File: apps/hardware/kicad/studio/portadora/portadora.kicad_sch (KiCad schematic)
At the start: 56 parts, among them J1 Teensy 4.1 izq, J10 USB-C 5V 3A, J11 OUT L 6.35, J12 OUT R 6.35, J13 PHONES 3.5 sleeve HP_VGND, J14 CV OUT 3.5, J2 Teensy 4.1 der, J3 USB host Teensy, J4 USB-A host, J5 Panel IDC 2x15, J6 Raspberry Pi pines 1-10, J7 IN L 6.35, J8 IN R 6.35, J9 Audio Shield LINE y HP, SW1 PAD 0 -10 -20 dB, U1 74AHCT1G125, U2 MCP6004

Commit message: feat(hardware): portadora con shield lado a lado y etapa de entrada validada por simulación
- Alimentación por JST-XH (J10) desde una placa USB-C de panel; USB-A host y USB de datos van
  en la tapa trasera con extensiones (se quitan J4, R1, R2).
- Audio Shield Rev D lado a lado, no apilado: zócalos J15/J16 que solo cablean 7, 8, 18–21, 23,
  3V3 y GND. Los pines 10–13 y 15 (encoders) quedan aislados del slot SD y del MEM.
- Etapa de entrada (theory/03-studio-input-stage.md): la escalera del pad se recalcula con la carga
  de R10+R12 (R5/R8 12.4k, R6/R9 5.23k) y el RC del CV OUT baja a 4.7k (1 % en 5 ms).
- Plan B: JP2–JP5 para saltar el MCP6004 si hiciera falta, y TP1–TP5 para diagnóstico.
- sim/input_stage_sim.py: ngspice de KiCad. Lee valores y topología del esquemático y verifica
  C1–C6; los seis pasan (sim/results.md).

Co-Authored-By: Claude Opus 5.5 <noreply@anthropic.com>
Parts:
- removed J10: USB-C 5V 3A, Connector_USB:USB_C_Receptacle_GCT_USB4125-xx-x_6P_TopMnt_Horizontal, symbol Connector:USB_C_Receptacle_PowerOnly_6P
- removed J4: USB-A host, Connector_USB:USB_A_Molex_67643_Horizontal, symbol Connector:USB_A
- removed R1, R2: 5.1k, Resistor_SMD:R_0603_1608Metric, symbol Device:R
- added J10: 5V desde USB-C de panel, Connector_JST:JST_XH_B2B-XH-A_1x02_P2.50mm_Vertical, symbol Connector_Generic:Conn_01x02
- added J15: Shield fila 13-5V, Connector_PinSocket_2.54mm:PinSocket_1x14_P2.54mm_Vertical, symbol Connector_Generic:Conn_01x14
- added J16: Shield fila 12-GND, Connector_PinSocket_2.54mm:PinSocket_1x14_P2.54mm_Vertical, symbol Connector_Generic:Conn_01x14
- added JP2: BYP L (sin U2), Jumper:SolderJumper-2_P1.3mm_Open_RoundedPad1.0x1.5mm, symbol Jumper:SolderJumper_2_Open
- added JP3: BYP R (sin U2), Jumper:SolderJumper-2_P1.3mm_Open_RoundedPad1.0x1.5mm, symbol Jumper:SolderJumper_2_Open
- added JP4: BYP VREF (sin U2), Jumper:SolderJumper-2_P1.3mm_Open_RoundedPad1.0x1.5mm, symbol Jumper:SolderJumper_2_Open
- added JP5: BYP CV (sin U2), Jumper:SolderJumper-2_P1.3mm_Open_RoundedPad1.0x1.5mm, symbol Jumper:SolderJumper_2_Open
- added TP1: VREF, TestPoint:TestPoint_Pad_D1.5mm, symbol Connector:TestPoint
- added TP2: BUF_L, TestPoint:TestPoint_Pad_D1.5mm, symbol Connector:TestPoint
- added TP3: BUF_R, TestPoint:TestPoint_Pad_D1.5mm, symbol Connector:TestPoint
- added TP4: CV_BUF, TestPoint:TestPoint_Pad_D1.5mm, symbol Connector:TestPoint
- added TP5: GND, TestPoint:TestPoint_Pad_D1.5mm, symbol Connector:TestPoint
- R18, R19: value 10k -> 4.7k
- R5, R8: value 10.2k -> 12.4k
- R6, R9: value 4.75k -> 5.23k
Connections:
- net +3V3: now also J15.12 (Pin_12)
- net BUF_L: now also JP2.2 (B), TP2.1
- net BUF_R: now also JP3.2 (B), TP3.1
- net CV_BUF: now also JP5.2 (B), TP4.1
- net CV_FILT: now also JP5.1 (A)
- net GND: now also J10.2 (Pin_2), J15.13 (Pin_13), J16.14 (Pin_14), TP5.1
- net PROT_L: now also JP2.1 (A)
- net PROT_R: now also JP3.1 (A)
- net VBUS_IN: now also J10.1 (Pin_1)
- net VREF: now also JP4.2 (B), TP1.1
- net VREF_DIV: now also JP4.1 (A)
- net I2S_MCLK: now reaches J2.4 (Pin_4)
- net I2S_MCLK: now also J15.11 (Pin_11)
- net I2S_BCLK: now reaches J2.6 (Pin_6)
- net I2S_BCLK: now also J15.9 (Pin_9)
- net I2S_LRCLK: now reaches J2.7 (Pin_7)
- net I2S_LRCLK: now also J15.8 (Pin_8)
- net I2C_SCL: now reaches J2.8 (Pin_8)
- net I2C_SCL: now also J15.7 (Pin_7)
- net I2C_SDA: now reaches J2.9 (Pin_9)
- net I2C_SDA: now also J15.6 (Pin_6)
- net I2S_RX: now reaches J1.10 (Pin_10)
- net I2S_RX: now also J16.5 (Pin_5)
- net I2S_TX: now reaches J1.9 (Pin_9)
- net I2S_TX: now also J16.6 (Pin_6)
- no-connect marks 20 -> 31
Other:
- note added: "NOTAS 1. Teensy 4.1: CORTAR el puente VUSB–VIN. Todo se alimenta de J10 (JST-XH desde una placa USB-C de panel, solo 5 V, con sus 5.1 kΩ en CC); el USB de la Teensy queda solo para datos (y MIDI por USB). 2. USB en la tapa trasera: USB-C de datos = extensión de panel a la micro-USB de la Teensy; USB-A host = extensión de panel a J3. J1/J2 = las dos filas de la Teensy (vista superior, USB arriba).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"
- note added: "PLAN B DE LA ETAPA DE ENTRADA (theory/03-studio-input-stage.md §6) JP2–JP5 abiertos de fábrica. Cerrarlos SOLO con U2 retirado o pedido DNP: un jumper cerrado con U2 montado une la salida del seguidor con su entrada. Diagnóstico sin señal: TP1 VREF, TP2 BUF_L y TP3 BUF_R = 1.65 V; TP4 sigue al duty del pin 29."
- note removed: "NOTAS 1. Teensy 4.1: CORTAR el puente VUSB–VIN de la Teensy. Todo se alimenta del USB-C de J10; el USB de la Teensy queda solo para datos (y MIDI por USB). 2. J1/J2 = las dos filas de la Teensy (vista superior, USB arriba). Izq: GND,0–12,3V3,24–32. Der: VIN,GND,3V3,23–13,GND,41–33. Los pines del Audio Shield (6,7,8,18,19,20,21,23) van por el apilado Teensy+Shield y quedan sin conexión en esta pla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"

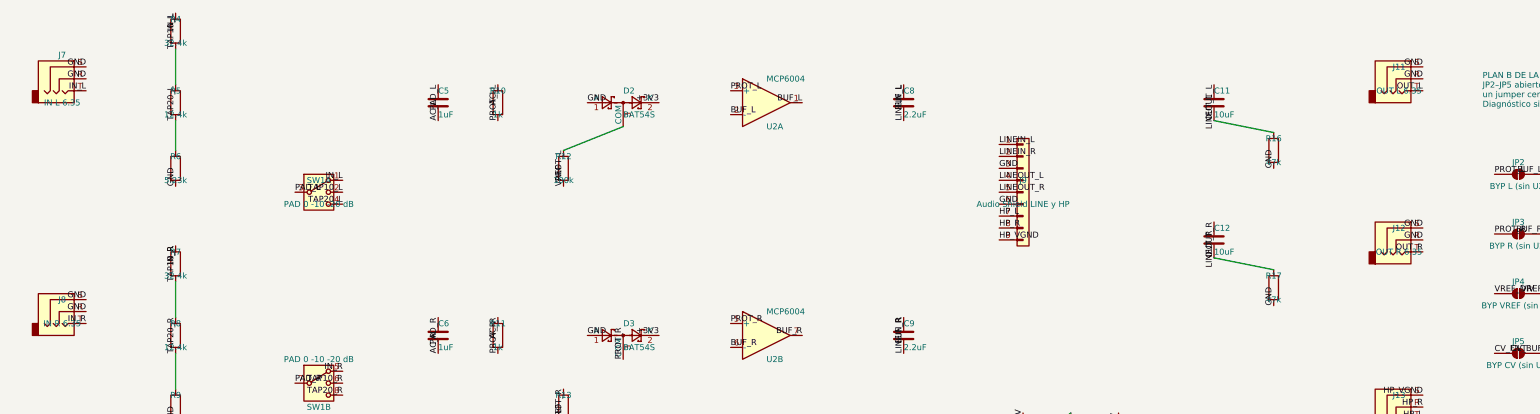
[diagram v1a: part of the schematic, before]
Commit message: feat(hardware): enclosure +15 mm, PCB-A de una cara y ubicación de la portadora
Enclosure (design/README.md, theory/02 §3 y §4.3–4.5), medido el módulo Freenove con la Pi:
- Cuña de 43/78 mm (+15 mm parejo, 12°): la portadora entra bajo la Pi con margen y hay más aire.
- Pantalla corrida 2.5 mm hacia atrás (centro y 114.9): el vidrio (120.8 × 76 × 7.6 mm) ya no se monta
  sobre PCB-K; ranuras de aire en y 155–165.
- Pi atornillada detrás de la Freenove, puertos hacia la derecha (adentro): se elimina la tapa de servicio.
- Jacks en una hilera baja soldados a la portadora (1/4" NRJ3HF-1); USB y palanca PAD de panel arriba.
  La placa trasera vertical se descartó antes de commit.

PCB-A: todos los SMD en la cara superior (ensamble Economic de una cara); vía propia para los GND del
JST; re-ruteada. DRC 0/0.

Portadora: tools/place_portadora.py (97 × 100 mm, jacks contra la pared, shield y entrada analógica al
medio, Teensy y alimentación adelante, J5/J6 al frente). DRC con paridad: 0 violaciones; falta rutear.
Herramientas: costura de GND que respeta agujeros e islas, route_board sin duplicar lo bloqueado,
sync_fp_fields con redes "unconnected" y atributos de BOM, trim_silk_outside.py.

Co-Authored-By: Claude Opus 5.5 <noreply@anthropic.com>
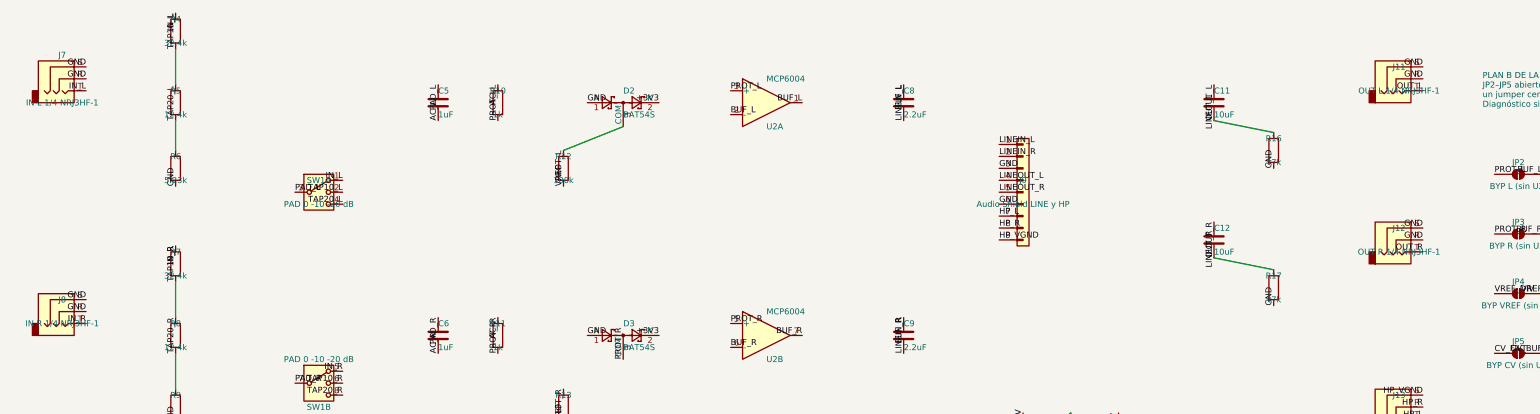
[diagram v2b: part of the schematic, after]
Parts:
- J11: value OUT L 6.35 -> OUT L 1/4 NRJ3HF-1; footprint Connector_Audio:Jack_6.35mm_Neutrik_NMJ6HFD2_Horizontal -> Connector_Audio:Jack_6.35mm_Neutrik_NRJ3HF-1_Horizontal
- J12: value OUT R 6.35 -> OUT R 1/4 NRJ3HF-1; footprint Connector_Audio:Jack_6.35mm_Neutrik_NMJ6HFD2_Horizontal -> Connector_Audio:Jack_6.35mm_Neutrik_NRJ3HF-1_Horizontal
- J7: value IN L 6.35 -> IN L 1/4 NRJ3HF-1; footprint Connector_Audio:Jack_6.35mm_Neutrik_NMJ6HFD2_Horizontal -> Connector_Audio:Jack_6.35mm_Neutrik_NRJ3HF-1_Horizontal
- J8: value IN R 6.35 -> IN R 1/4 NRJ3HF-1; footprint Connector_Audio:Jack_6.35mm_Neutrik_NMJ6HFD2_Horizontal -> Connector_Audio:Jack_6.35mm_Neutrik_NRJ3HF-1_Horizontal
- JP1, JP2, JP3, JP4, JP5, TP1, TP2, TP3, TP4, TP5: now left out of the parts list
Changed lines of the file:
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@@
 		(body_style 1)
 		(exclude_from_sim no)
-		(in_bom yes)
+		(in_bom no)
 		(on_board yes)
-		(in_pos_files yes)
+		(in_pos_files no)
 		(dnp no)
 		(property "Reference" "JP1"
@@
 			)
 		)
-		(property "Value" "IN L 6.35"
+		(property "Value" "IN L 1/4 NRJ3HF-1"
 			(at 25.4 185.42 0)
 			(show_name no)
@@
 			)
 		)
-		(property "Footprint" "Connector_Audio:Jack_6.35mm_Neutrik_NMJ6HFD2_Horizontal"
+		(property "Footprint" "Connector_Audio:Jack_6.35mm_Neutrik_NRJ3HF-1_Horizontal"
 			(at 25.4 180.34 0)
 			(hide yes)
@@
 			)
 		)
-		(property "Value" "IN R 6.35"
+		(property "Value" "IN R 1/4 NRJ3HF-1"
 			(at 25.4 232.41 0)
 			(show_name no)
@@
 			)
 		)
-		(property "Footprint" "Connector_Audio:Jack_6.35mm_Neutrik_NMJ6HFD2_Horizontal"
+		(property "Footprint" "Connector_Audio:Jack_6.35mm_Neutrik_NRJ3HF-1_Horizontal"
 			(at 25.4 229.87 0)
 			(hide yes)
@@
 			)
 		)
-		(property "Value" "OUT L 6.35"
+		(property "Value" "OUT L 1/4 NRJ3HF-1"
 			(at 309.88 182.88 0)
 			(show_name no)
@@
 			)
 		)
-		(property "Footprint" "Connector_Audio:Jack_6.35mm_Neutrik_NMJ6HFD2_Horizontal"
+		(property "Footprint" "Connector_Audio:Jack_6.35mm_Neutrik_NRJ3HF-1_Horizontal"
 			(at 309.88 180.34 0)
 			(hide yes)
@@
 			)
 		)
-		(property "Value" "OUT R 6.35"
+		(property "Value" "OUT R 1/4 NRJ3HF-1"
 			(at 309.88 217.17 0)
 			(show_name no)
@@
 			)
 		)
-		(property "Footprint" "Connector_Audio:Jack_6.35mm_Neutrik_NMJ6HFD2_Horizontal"
+		(property "Footprint" "Connector_Audio:Jack_6.35mm_Neutrik_NRJ3HF-1_Horizontal"
 			(at 309.88 214.63 0)
 			(hide yes)
@@
 		(body_style 1)
 		(exclude_from_sim no)
-		(in_bom yes)
+		(in_bom no)
 		(on_board yes)
-		(in_pos_files yes)
+		(in_pos_files no)
 		(dnp no)
 		(property "Reference" "JP2"
@@
 		(body_style 1)
 		(exclude_from_sim no)
-		(in_bom yes)
+		(in_bom no)
 		(on_board yes)
-		(in_pos_files yes)
+		(in_pos_files no)
 		(dnp no)
 		(property "Reference" "JP3"
@@
 		(body_style 1)
 		(exclude_from_sim no)
-		(in_bom yes)
+		(in_bom no)
 		(on_board yes)
-		(in_pos_files yes)
+		(in_pos_files no)
 		(dnp no)
 		(property "Reference" "JP4"
@@
 		(body_style 1)
 		(exclude_from_sim no)
-		(in_bom yes)
+		(in_bom no)
 		(on_board yes)
-		(in_pos_files yes)
+		(in_pos_files no)
 		(dnp no)
 		(property "Reference" "JP5"
@@
 		(body_style 1)
 		(exclude_from_sim no)
-		(in_bom yes)
+		(in_bom no)
 		(on_board yes)
-		(in_pos_files yes)
+		(in_pos_files no)
 		(dnp no)
 		(property "Reference" "TP1"
@@
 		(body_style 1)
 		(exclude_from_sim no)
-		(in_bom yes)
+		(in_bom no)
 		(on_board yes)
-		(in_pos_files yes)
+		(in_pos_files no)
 		(dnp no)
 		(property "Reference" "TP2"
@@
 		(body_style 1)
 		(exclude_from_sim no)
-		(in_bom yes)
+		(in_bom no)
 		(on_board yes)
-		(in_pos_files yes)
+		(in_pos_files no)
 		(dnp no)
 		(property "Reference" "TP3"
@@
 		(body_style 1)
 		(exclude_from_sim no)
-		(in_bom yes)
+		(in_bom no)
 		(on_board yes)
-		(in_pos_files yes)
+		(in_pos_files no)
 		(dnp no)
 		(property "Reference" "TP4"
@@
 		(body_style 1)
 		(exclude_from_sim no)
-		(in_bom yes)
+		(in_bom no)
 		(on_board yes)
-		(in_pos_files yes)
+		(in_pos_files no)
 		(dnp no)
 		(property "Reference" "TP5"

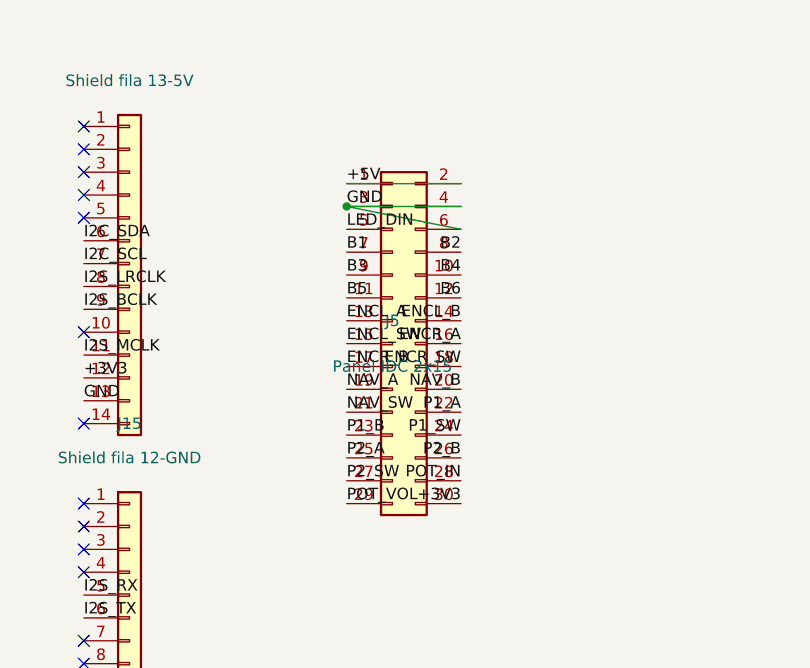
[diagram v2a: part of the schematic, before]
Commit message: feat(hardware): portadora ruteada (DRC limpio) y pinout del IDC reordenado
- Portadora: ruteo completo, DRC con paridad de esquemático 0/0/0 contra reglas de JLCPCB.
  +5V de F1 a la Pi en ~40 mm con una vía; sin paralelos audio↔digital a <1 mm.
- IDC 2×15 (PCB-A J2 ↔ portadora J5): pines ordenados por la X del pin de la Teensy al que van,
  para que el bus salga del conector sin cruces. Ambos esquemáticos re-etiquetados (ERC limpio),
  PCB-A re-ruteada (DRC 0/0/0). Tablas y razón en theory/02 §6.2.
- Herramientas: grid_route (Dijkstra en grilla 0.1 mm, 2 capas), finish_routing (rip-up and
  reroute de lo que deja Freerouting), clean_vias, add_gnd_escapes, fix_portadora_gnd,
  set_idc_pinout y build_portadora.sh (pipeline completo reproducible).

Co-Authored-By: Claude Opus 5.5 <noreply@anthropic.com>
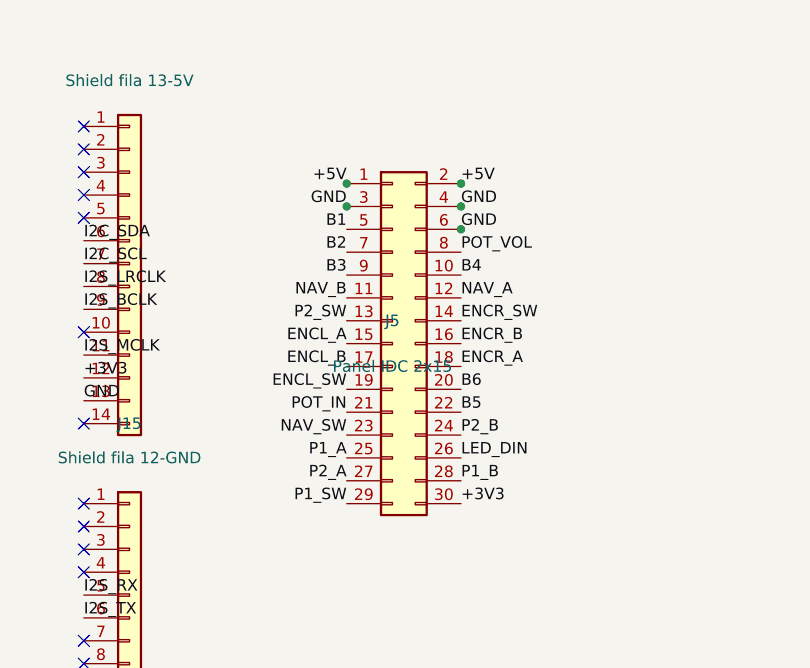
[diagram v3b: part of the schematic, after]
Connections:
- net B1: now also J5.5 (Pin_5); no longer J5.7 (Pin_7)
- net B2: now also J5.7 (Pin_7); no longer J5.8 (Pin_8)
- net B5: now also J5.22 (Pin_22); no longer J5.11 (Pin_11)
- net B6: now also J5.20 (Pin_20); no longer J5.12 (Pin_12)
- net ENCL_A: now also J5.15 (Pin_15); no longer J5.13 (Pin_13)
- net ENCL_B: now also J5.17 (Pin_17); no longer J5.14 (Pin_14)
- net ENCL_SW: now also J5.19 (Pin_19); no longer J5.15 (Pin_15)
- net ENCR_A: now also J5.18 (Pin_18); no longer J5.16 (Pin_16)
- net ENCR_B: now also J5.16 (Pin_16); no longer J5.17 (Pin_17)
- net ENCR_SW: now also J5.14 (Pin_14); no longer J5.18 (Pin_18)
- net LED_DIN: now also J5.26 (Pin_26); no longer J5.5 (Pin_5)
- net NAV_A: now also J5.12 (Pin_12); no longer J5.19 (Pin_19)
- net NAV_B: now also J5.11 (Pin_11); no longer J5.20 (Pin_20)
- net NAV_SW: now also J5.23 (Pin_23); no longer J5.21 (Pin_21)
- net P1_A: now also J5.25 (Pin_25); no longer J5.22 (Pin_22)
- net P1_B: now also J5.28 (Pin_28); no longer J5.23 (Pin_23)
- net P1_SW: now also J5.29 (Pin_29); no longer J5.24 (Pin_24)
- net P2_A: now also J5.27 (Pin_27); no longer J5.25 (Pin_25)
- net P2_B: now also J5.24 (Pin_24); no longer J5.26 (Pin_26)
- net P2_SW: now also J5.13 (Pin_13); no longer J5.27 (Pin_27)
- net POT_IN: now also J5.21 (Pin_21); no longer J5.28 (Pin_28)
- net POT_VOL: now also J5.8 (Pin_8); no longer J5.29 (Pin_29)
